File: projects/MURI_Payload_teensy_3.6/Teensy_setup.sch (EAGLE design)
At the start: 52 parts, among them IC1 DS18B20, IC2 DS18B20, IC3 74ALS08N, IC4 DS18B20, IC5 DS18B20, U2 MS560702BA03-50

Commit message: Added Xbee and UBlox.
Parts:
- removed COPERNICUS_II: COPERNICUSSMD, SparkFun-GPS:COPERNICUSSMD
- removed IC3: 74ALS08N, 74xx-us:74ALS08N
- removed J1, J2: (no value), SparkFun-Connectors:CONN_03
- added UBLOX, XBEE: (no value), con-lstb:MA04-1
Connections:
- removed net GPS_RX: COPERNICUS_II.RXD-B, U$1.10/CS
- removed net GPS_TX: COPERNICUS_II.TXD-B, U$1.9/CS
- removed net N$14: IC3B.O, J2.1
- removed net N$15: IC3A.O, J1.1
- removed net SERVO_1: IC3B.I0, IC3B.I1, U$1.17/A3
- removed net SERVO_2: IC3A.I0, IC3A.I1, U$1.16/A2
- new net DIN: U$1.33/A14, XBEE.1
- new net DOUT: U$1.34/A15, XBEE.2
- new net RX: U$1.10/CS, UBLOX.2
- new net TX: U$1.9/CS, UBLOX.3
- net 5V: now also XBEE.3; no longer J1.2, J2.2
- net GND: now also UBLOX.4, XBEE.4; no longer COPERNICUS_II.GND@1, J1.3, J2.3
- net VCC: now also UBLOX.1; no longer COPERNICUS_II.RESERVED2, COPERNICUS_II.VCC

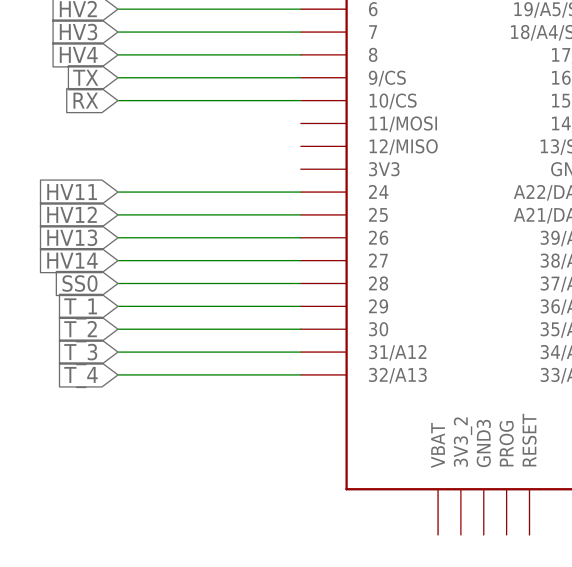
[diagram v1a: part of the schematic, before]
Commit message: Got rid of an assigned pin from a depricated sensor.
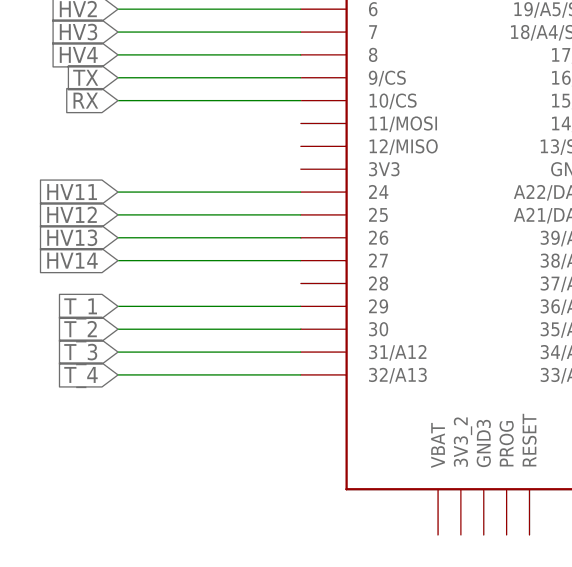
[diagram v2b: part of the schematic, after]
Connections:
- removed net SS0: U$1.28
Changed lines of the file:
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@@
-</segment>
-</net>
-<net name="SS0" class="0">
-<segment>
-<pinref part="U$1" gate="G$1" pin="28"/>
-<wire x1="-172.72" y1="78.74" x2="-193.04" y2="78.74" width="0.1524" layer="91"/>
-<label x="-193.04" y="78.74" size="1.778" layer="95" rot="MR0" xref="yes"/>
 </segment>
 </net>

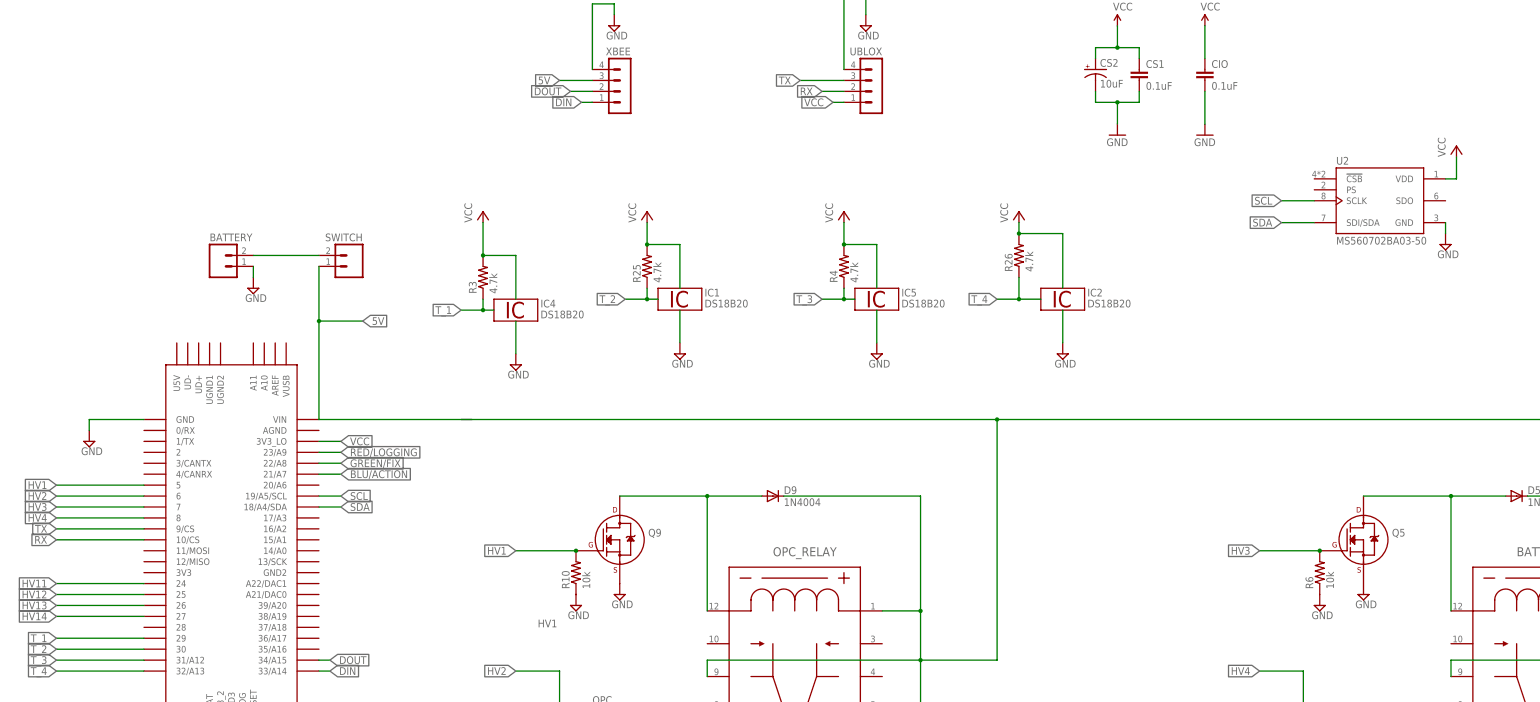
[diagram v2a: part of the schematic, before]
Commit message: Fixed wiring of MS5607 and updated external SMART schematic.
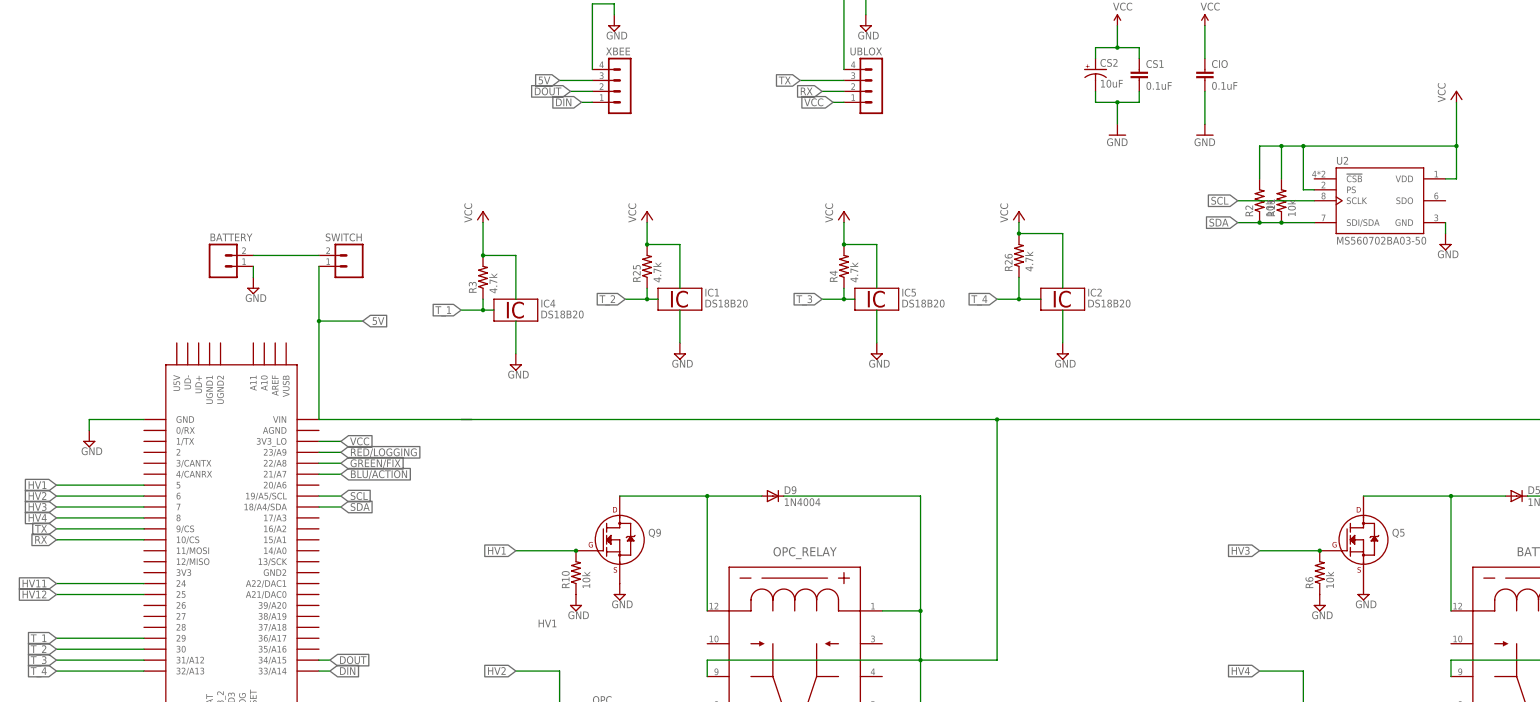
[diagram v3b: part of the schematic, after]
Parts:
- added R11, R2: 10k, rcl:R-US_0204/7
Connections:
- removed net HV13: U$1.26
- removed net HV14: U$1.27
- net SDA: now also R11.1, R2.1
- net VCC: now also R11.2, R2.2, U2.PS
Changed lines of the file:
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@@
 <part name="SUPPLY15" library="supply2" library_urn="urn:adsk.eagle:library:372" deviceset="GND" device=""/>
 <part name="SUPPLY16" library="supply2" library_urn="urn:adsk.eagle:library:372" deviceset="GND" device=""/>
-<part name="R5" library="rcl" library_urn="urn:adsk.eagle:library:334" deviceset="R-US_" device="0207/7" package3d_urn="urn:adsk.eagle:package:23493/1" value="10k"/>
-<part name="R6" library="rcl" library_urn="urn:adsk.eagle:library:334" deviceset="R-US_" device="0207/7" package3d_urn="urn:adsk.eagle:package:23493/1" value="10k"/>
+<part name="R5" library="rcl" library_urn="urn:adsk.eagle:library:334" deviceset="R-US_" device="0207/7" package3d_urn="urn:adsk.eagle:package:23493/2" value="10k"/>
+<part name="R6" library="rcl" library_urn="urn:adsk.eagle:library:334" deviceset="R-US_" device="0207/7" package3d_urn="urn:adsk.eagle:package:23493/2" value="10k"/>
 <part name="BATTERY_HEATER" library="con-amp-quick" library_urn="urn:adsk.eagle:library:125" deviceset="M02" device="" package3d_urn="urn:adsk.eagle:package:5956/1"/>
 <part name="SUPPLY17" library="supply2" library_urn="urn:adsk.eagle:library:372" deviceset="GND" device=""/>
@@
 <part name="SUPPLY21" library="supply2" library_urn="urn:adsk.eagle:library:372" deviceset="GND" device=""/>
 <part name="SUPPLY22" library="supply2" library_urn="urn:adsk.eagle:library:372" deviceset="GND" device=""/>
-<part name="R7" library="rcl" library_urn="urn:adsk.eagle:library:334" deviceset="R-US_" device="0207/7" package3d_urn="urn:adsk.eagle:package:23493/1" value="10k"/>
-<part name="R8" library="rcl" library_urn="urn:adsk.eagle:library:334" deviceset="R-US_" device="0207/7" package3d_urn="urn:adsk.eagle:package:23493/1" value="10k"/>
+<part name="R7" library="rcl" library_urn="urn:adsk.eagle:library:334" deviceset="R-US_" device="0207/7" package3d_urn="urn:adsk.eagle:package:23493/2" value="10k"/>
+<part name="R8" library="rcl" library_urn="urn:adsk.eagle:library:334" deviceset="R-US_" device="0207/7" package3d_urn="urn:adsk.eagle:package:23493/2" value="10k"/>
 <part name="OPC_HEAT" library="con-amp-quick" library_urn="urn:adsk.eagle:library:125" deviceset="M02" device="" package3d_urn="urn:adsk.eagle:package:5956/1"/>
 <part name="SUPPLY23" library="supply2" library_urn="urn:adsk.eagle:library:372" deviceset="GND" device=""/>
@@
 <part name="SUPPLY27" library="supply2" library_urn="urn:adsk.eagle:library:372" deviceset="GND" device=""/>
 <part name="SUPPLY28" library="supply2" library_urn="urn:adsk.eagle:library:372" deviceset="GND" device=""/>
-<part name="R9" library="rcl" library_urn="urn:adsk.eagle:library:334" deviceset="R-US_" device="0207/7" package3d_urn="urn:adsk.eagle:package:23493/1" value="10k"/>
-<part name="R10" library="rcl" library_urn="urn:adsk.eagle:library:334" deviceset="R-US_" device="0207/7" package3d_urn="urn:adsk.eagle:package:23493/1" value="10k"/>
+<part name="R9" library="rcl" library_urn="urn:adsk.eagle:library:334" deviceset="R-US_" device="0207/7" package3d_urn="urn:adsk.eagle:package:23493/2" value="10k"/>
+<part name="R10" library="rcl" library_urn="urn:adsk.eagle:library:334" deviceset="R-US_" device="0207/7" package3d_urn="urn:adsk.eagle:package:23493/2" value="10k"/>
 <part name="OPC" library="con-amp-quick" library_urn="urn:adsk.eagle:library:125" deviceset="M02" device="" package3d_urn="urn:adsk.eagle:package:5956/1"/>
 <part name="SUPPLY29" library="supply2" library_urn="urn:adsk.eagle:library:372" deviceset="GND" device=""/>
@@
 <part name="XBEE" library="con-lstb" library_urn="urn:adsk.eagle:library:162" deviceset="MA04-1" device="" package3d_urn="urn:adsk.eagle:package:8337/1"/>
 <part name="SUPPLY18" library="supply2" library_urn="urn:adsk.eagle:library:372" deviceset="GND" device=""/>
+<part name="R2" library="rcl" library_urn="urn:adsk.eagle:library:334" deviceset="R-US_" device="0204/7" package3d_urn="urn:adsk.eagle:package:23498/2" value="10k"/>
+<part name="R11" library="rcl" library_urn="urn:adsk.eagle:library:334" deviceset="R-US_" device="0204/7" package3d_urn="urn:adsk.eagle:package:23498/2" value="10k"/>
 </parts>
 <sheets>
@@
 <attribute name="VALUE" x="127.635" y="164.465" size="1.778" layer="96"/>
 </instance>
-<instance part="P+2" gate="VCC" x="132.08" y="190.5" smashed="yes">
-<attribute name="VALUE" x="129.54" y="187.96" size="1.778" layer="96" rot="R90"/>
+<instance part="P+2" gate="VCC" x="132.08" y="203.2" smashed="yes">
+<attribute name="VALUE" x="129.54" y="200.66" size="1.778" layer="96" rot="R90"/>
 </instance>
 <instance part="UBLOX" gate="1" x="-2.54" y="205.74" smashed="yes" rot="MR0">
@@
 <instance part="SUPPLY18" gate="GND" x="-63.5" y="218.44" smashed="yes">
 <attribute name="VALUE" x="-65.405" y="215.265" size="1.778" layer="96"/>
+</instance>
+<instance part="R2" gate="G$1" x="86.36" y="177.8" smashed="yes" rot="R90">
+<attribute name="NAME" x="84.8614" y="173.99" size="1.778" layer="95" rot="R90"/>
+<attribute name="VALUE" x="89.662" y="173.99" size="1.778" layer="96" rot="R90"/>
+</instance>
+<instance part="R11" gate="G$1" x="91.44" y="177.8" smashed="yes" rot="R90">
+<attribute name="NAME" x="89.9414" y="173.99" size="1.778" layer="95" rot="R90"/>
+<attribute name="VALUE" x="94.742" y="173.99" size="1.778" layer="96" rot="R90"/>
 </instance>
 </instances>
@@
 <wire x1="-172.72" y1="86.36" x2="-193.04" y2="86.36" width="0.1524" layer="91"/>
 <label x="-193.04" y="86.36" size="1.778" layer="95" rot="MR0" xref="yes"/>
-</segment>
-</net>
-<net name="HV13" class="0">
-<segment>
-<pinref part="U$1" gate="G$1" pin="26"/>
-<wire x1="-172.72" y1="83.82" x2="-193.04" y2="83.82" width="0.1524" layer="91"/>
-<label x="-193.04" y="83.82" size="1.778" layer="95" rot="MR0" xref="yes"/>
-</segment>
-</net>
-<net name="HV14" class="0">
-<segment>
-<pinref part="U$1" gate="G$1" pin="27"/>
-<wire x1="-172.72" y1="81.28" x2="-193.04" y2="81.28" width="0.1524" layer="91"/>
-<label x="-193.04" y="81.28" size="1.778" layer="95" rot="MR0" xref="yes"/>
 </segment>
 </net>
@@
 <segment>
 <pinref part="U2" gate="G$1" pin="SCLK"/>
-<wire x1="99.06" y1="177.8" x2="91.44" y2="177.8" width="0.1524" layer="91"/>
-<label x="91.44" y="177.8" size="1.778" layer="95" rot="MR0" xref="yes"/>
+<wire x1="99.06" y1="177.8" x2="81.28" y2="177.8" width="0.1524" layer="91"/>
+<label x="81.28" y="177.8" size="1.778" layer="95" rot="MR0" xref="yes"/>
 </segment>
 </net>
@@
 <pinref part="U2" gate="G$1" pin="SDI/SDA"/>
 <wire x1="99.06" y1="172.72" x2="91.44" y2="172.72" width="0.1524" layer="91"/>
-<label x="91.44" y="172.72" size="1.778" layer="95" rot="MR0" xref="yes"/>
+<label x="81.28" y="172.72" size="1.778" layer="95" rot="MR0" xref="yes"/>
+<pinref part="R2" gate="G$1" pin="1"/>
+<wire x1="91.44" y1="172.72" x2="86.36" y2="172.72" width="0.1524" layer="91"/>
+<wire x1="86.36" y1="172.72" x2="81.28" y2="172.72" width="0.1524" layer="91"/>
+<junction x="86.36" y="172.72"/>
+<pinref part="R11" gate="G$1" pin="1"/>
+<junction x="91.44" y="172.72"/>
 </segment>
 </net>
@@
 <pinref part="P+2" gate="VCC" pin="VCC"/>
 <wire x1="129.54" y1="182.88" x2="132.08" y2="182.88" width="0.1524" layer="91"/>
-<wire x1="132.08" y1="182.88" x2="132.08" y2="187.96" width="0.1524" layer="91"/>
+<wire x1="132.08" y1="182.88" x2="132.08" y2="190.5" width="0.1524" layer="91"/>
+<wire x1="132.08" y1="190.5" x2="132.08" y2="200.66" width="0.1524" layer="91"/>
+<wire x1="132.08" y1="190.5" x2="96.52" y2="190.5" width="0.1524" layer="91"/>
+<junction x="132.08" y="190.5"/>
+<pinref part="R2" gate="G$1" pin="2"/>
+<wire x1="96.52" y1="190.5" x2="91.44" y2="190.5" width="0.1524" layer="91"/>
+<wire x1="91.44" y1="190.5" x2="86.36" y2="190.5" width="0.1524" layer="91"/>
+<wire x1="86.36" y1="190.5" x2="86.36" y2="182.88" width="0.1524" layer="91"/>
+<pinref part="R11" gate="G$1" pin="2"/>
+<wire x1="91.44" y1="182.88" x2="91.44" y2="190.5" width="0.1524" layer="91"/>
+<junction x="91.44" y="190.5"/>
+<pinref part="U2" gate="G$1" pin="PS"/>
+<wire x1="99.06" y1="180.34" x2="96.52" y2="180.34" width="0.1524" layer="91"/>
+<wire x1="96.52" y1="180.34" x2="96.52" y2="190.5" width="0.1524" layer="91"/>
+<junction x="96.52" y="190.5"/>
 </segment>
 <segment>
@@
 packages will not be understood (or retained) with this version.
 </note>
+<note version="8.4" severity="warning">
+Since Version 8.4, EAGLE supports properties for SPICE simulation.
+Probes in schematics and SPICE mapping objects found in parts and library devices
+will not be understood with this version. Update EAGLE to the latest version
+for full support of SPICE simulation.
+</note>
 </compatibility>

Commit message: Added edits to teensy 3.6 schematic for the plantower. Added stuff from EAGLE intro presentation.
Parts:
- added B1: SPARKFUN_LOGIC_LEVEL_CONVERTER, SparkFun-Boards:SPARKFUN_LOGIC_LEVEL_CONVERTER
- added PLANTOWER: (no value), SparkFun-Connectors:CONN_08"
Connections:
- new net TX_PT_HIGH: B1.HV_TXO_1, U$1.0/RX
- new net TX_PT_LOW: B1.LV_TXI_1, PLANTOWER.4
- net 5V2: now also B1.HV
- net GND: now also B1.GND, B1.GND@2, PLANTOWER.2
- net VCC: now also B1.LV, PLANTOWER.1
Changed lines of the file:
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@@
 <part name="R2" library="rcl" library_urn="urn:adsk.eagle:library:334" deviceset="R-US_" device="0204/7" package3d_urn="urn:adsk.eagle:package:23498/2" value="10k"/>
 <part name="R11" library="rcl" library_urn="urn:adsk.eagle:library:334" deviceset="R-US_" device="0204/7" package3d_urn="urn:adsk.eagle:package:23498/2" value="10k"/>
+<part name="B1" library="SparkFun-Boards" library_urn="urn:adsk.eagle:library:509" deviceset="SPARKFUN_LOGIC_LEVEL_CONVERTER" device="" package3d_urn="urn:adsk.eagle:package:37318/1"/>
+<part name="PLANTOWER" library="SparkFun-Connectors" library_urn="urn:adsk.eagle:library:513" deviceset="CONN_08" device="&quot;" package3d_urn="urn:adsk.eagle:package:38138/1"/>
+<part name="SUPPLY1" library="supply2" library_urn="urn:adsk.eagle:library:372" deviceset="GND" device=""/>
+<part name="SUPPLY24" library="supply2" library_urn="urn:adsk.eagle:library:372" deviceset="GND" device=""/>
+<part name="SUPPLY30" library="supply2" library_urn="urn:adsk.eagle:library:372" deviceset="GND" device=""/>
 </parts>
 <sheets>
@@
 </instance>
 <instance part="U$1" gate="G$1" x="-152.4" y="114.3" smashed="yes"/>
-<instance part="SUPPLY7" gate="GND" x="-185.42" y="121.92" smashed="yes">
-<attribute name="VALUE" x="-187.325" y="118.745" size="1.778" layer="96"/>
+<instance part="SUPPLY7" gate="GND" x="-180.34" y="134.62" smashed="yes">
+<attribute name="VALUE" x="-182.245" y="131.445" size="1.778" layer="96"/>
 </instance>
 <instance part="BATTERY_HEATER_RELAY" gate="A" x="151.13" y="69.85" smashed="yes">
@@
 <attribute name="NAME" x="89.9414" y="173.99" size="1.778" layer="95" rot="R90"/>
 <attribute name="VALUE" x="94.742" y="173.99" size="1.778" layer="96" rot="R90"/>
+</instance>
+<instance part="B1" gate="G$1" x="259.08" y="160.02" smashed="yes">
+<attribute name="NAME" x="254" y="170.434" size="1.778" layer="95" font="vector"/>
+<attribute name="VALUE" x="254" y="152.146" size="1.778" layer="95" font="vector" align="top-left"/>
+</instance>
+<instance part="PLANTOWER" gate="G$1" x="172.72" y="165.1" smashed="yes">
+<attribute name="VALUE" x="167.64" y="152.654" size="1.778" layer="96" font="vector"/>
+<attribute name="NAME" x="167.64" y="178.308" size="1.778" layer="95" font="vector"/>
+</instance>
+<instance part="SUPPLY1" gate="GND" x="180.34" y="147.32" smashed="yes">
+<attribute name="VALUE" x="178.435" y="144.145" size="1.778" layer="96"/>
+</instance>
+<instance part="SUPPLY24" gate="GND" x="236.22" y="144.78" smashed="yes">
+<attribute name="VALUE" x="234.315" y="141.605" size="1.778" layer="96"/>
+</instance>
+<instance part="SUPPLY30" gate="GND" x="284.48" y="142.24" smashed="yes">
+<attribute name="VALUE" x="282.575" y="139.065" size="1.778" layer="96"/>
 </instance>
 </instances>
@@
 <segment>
 <pinref part="U$1" gate="G$1" pin="GND"/>
-<wire x1="-172.72" y1="127" x2="-185.42" y2="127" width="0.1524" layer="91"/>
+<wire x1="-172.72" y1="127" x2="-172.72" y2="137.16" width="0.1524" layer="91"/>
 <pinref part="SUPPLY7" gate="GND" pin="GND"/>
-<wire x1="-185.42" y1="127" x2="-185.42" y2="124.46" width="0.1524" layer="91"/>
+<wire x1="-172.72" y1="137.16" x2="-180.34" y2="137.16" width="0.1524" layer="91"/>
 </segment>
 <segment>
@@
 <wire x1="-63.5" y1="223.52" x2="-63.5" y2="220.98" width="0.1524" layer="91"/>
 <pinref part="SUPPLY18" gate="GND" pin="GND"/>
+</segment>
+<segment>
+<pinref part="PLANTOWER" gate="G$1" pin="2"/>
+<wire x1="177.8" y1="160.02" x2="180.34" y2="160.02" width="0.1524" layer="91"/>
+<wire x1="180.34" y1="160.02" x2="180.34" y2="149.86" width="0.1524" layer="91"/>
+<pinref part="SUPPLY1" gate="GND" pin="GND"/>
+</segment>
+<segment>
+<pinref part="B1" gate="G$1" pin="GND"/>
+<wire x1="241.3" y1="160.02" x2="236.22" y2="160.02" width="0.1524" layer="91"/>
+<wire x1="236.22" y1="160.02" x2="236.22" y2="147.32" width="0.1524" layer="91"/>
+<pinref part="SUPPLY24" gate="GND" pin="GND"/>
+</segment>
+<segment>
+<pinref part="B1" gate="G$1" pin="GND@2"/>
+<wire x1="274.32" y1="160.02" x2="284.48" y2="160.02" width="0.1524" layer="91"/>
+<wire x1="284.48" y1="160.02" x2="284.48" y2="144.78" width="0.1524" layer="91"/>
+<pinref part="SUPPLY30" gate="GND" pin="GND"/>
 </segment>
 </net>
@@
 <junction x="25.4" y="127"/>
 <wire x1="368.3" y1="71.12" x2="368.3" y2="127" width="0.1524" layer="91"/>
-<wire x1="368.3" y1="127" x2="193.04" y2="127" width="0.1524" layer="91"/>
+<wire x1="368.3" y1="127" x2="299.72" y2="127" width="0.1524" layer="91"/>
 <junction x="193.04" y="127"/>
+<pinref part="B1" gate="G$1" pin="HV"/>
+<wire x1="299.72" y1="127" x2="193.04" y2="127" width="0.1524" layer="91"/>
+<wire x1="274.32" y1="162.56" x2="299.72" y2="162.56" width="0.1524" layer="91"/>
+<wire x1="299.72" y1="162.56" x2="299.72" y2="127" width="0.1524" layer="91"/>
+<junction x="299.72" y="127"/>
 </segment>
 </net>
@@
 <label x="-12.7" y="200.66" size="1.778" layer="95" rot="MR0" xref="yes"/>
 </segment>
+<segment>
+<pinref part="PLANTOWER" gate="G$1" pin="1"/>
+<wire x1="177.8" y1="157.48" x2="182.88" y2="157.48" width="0.1524" layer="91"/>
+<label x="182.88" y="157.48" size="1.778" layer="95" xref="yes"/>
+</segment>
+<segment>
+<pinref part="B1" gate="G$1" pin="LV"/>
+<wire x1="241.3" y1="162.56" x2="233.68" y2="162.56" width="0.1524" layer="91"/>
+<label x="233.68" y="162.56" size="1.778" layer="95" rot="MR0" xref="yes"/>
+</segment>
 </net>
 <net name="N$1" class="0">
@@
 </segment>
 </net>
+<net name="TX_PT_HIGH" class="0">
+<segment>
+<pinref part="B1" gate="G$1" pin="HV_TXO_1"/>
+<wire x1="274.32" y1="167.64" x2="281.94" y2="167.64" width="0.1524" layer="91"/>
+<label x="281.94" y="167.64" size="1.778" layer="95" xref="yes"/>
+</segment>
+<segment>
+<pinref part="U$1" gate="G$1" pin="0/RX"/>
+<wire x1="-172.72" y1="124.46" x2="-177.8" y2="124.46" width="0.1524" layer="91"/>
+<label x="-177.8" y="124.46" size="1.778" layer="95" rot="MR0" xref="yes"/>
+</segment>
+</net>
+<net name="TX_PT_LOW" class="0">
+<segment>
+<pinref part="B1" gate="G$1" pin="LV_TXI_1"/>
+<wire x1="241.3" y1="167.64" x2="233.68" y2="167.64" width="0.1524" layer="91"/>
+<label x="233.68" y="167.64" size="1.778" layer="95" rot="MR0" xref="yes"/>
+</segment>
+<segment>
+<pinref part="PLANTOWER" gate="G$1" pin="4"/>
+<wire x1="177.8" y1="165.1" x2="182.88" y2="165.1" width="0.1524" layer="91"/>
+<label x="182.88" y="165.1" size="1.778" layer="95" xref="yes"/>
+</segment>
+</net>
